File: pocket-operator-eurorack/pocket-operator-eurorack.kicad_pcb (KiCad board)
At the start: 2 copper layers, 70.8 x 128.5 mm, 0 parts

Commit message: kicad silkscreen updated
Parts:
- added G***: LOGO, pocket-operator-eurorack:hook_fill, F.Cu at (31.6, 8.89)
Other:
- outline, holes or cut-outs redrawn

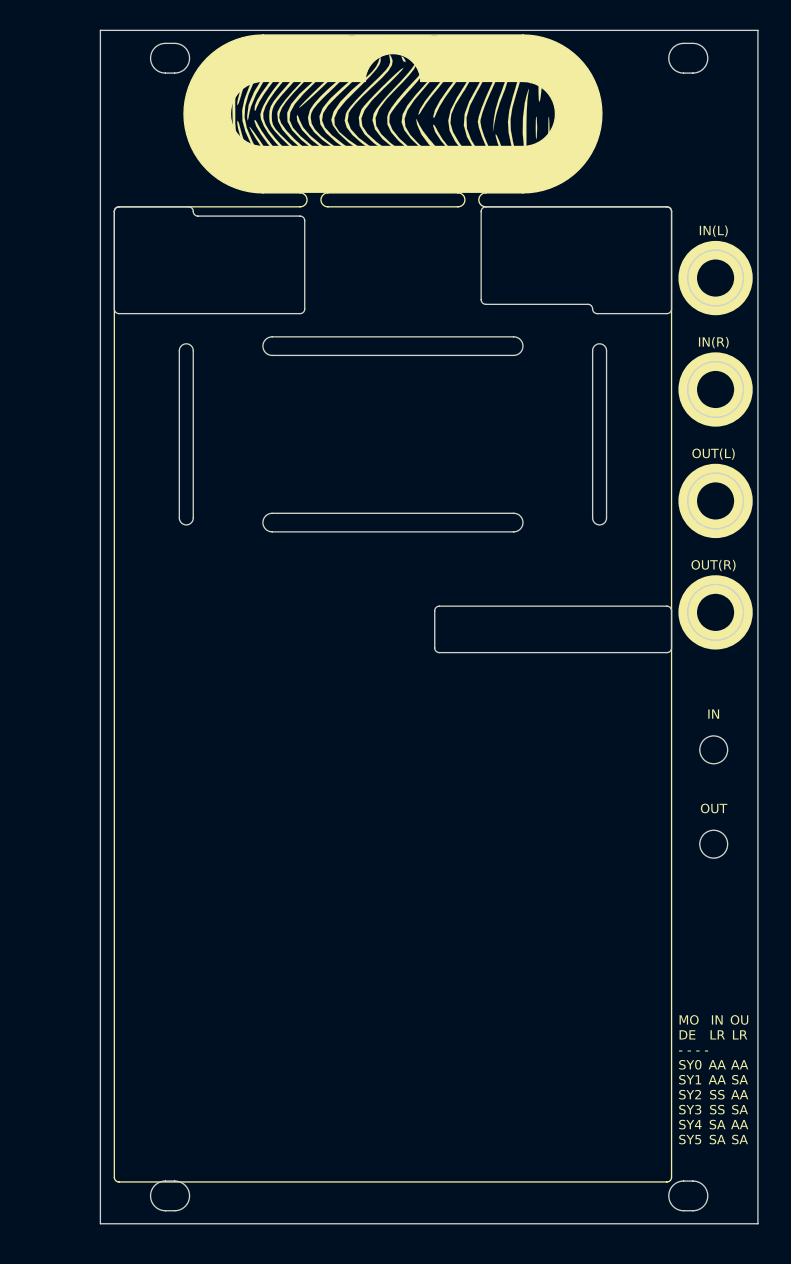
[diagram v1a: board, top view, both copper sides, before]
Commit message: front silkscreen artwork finished
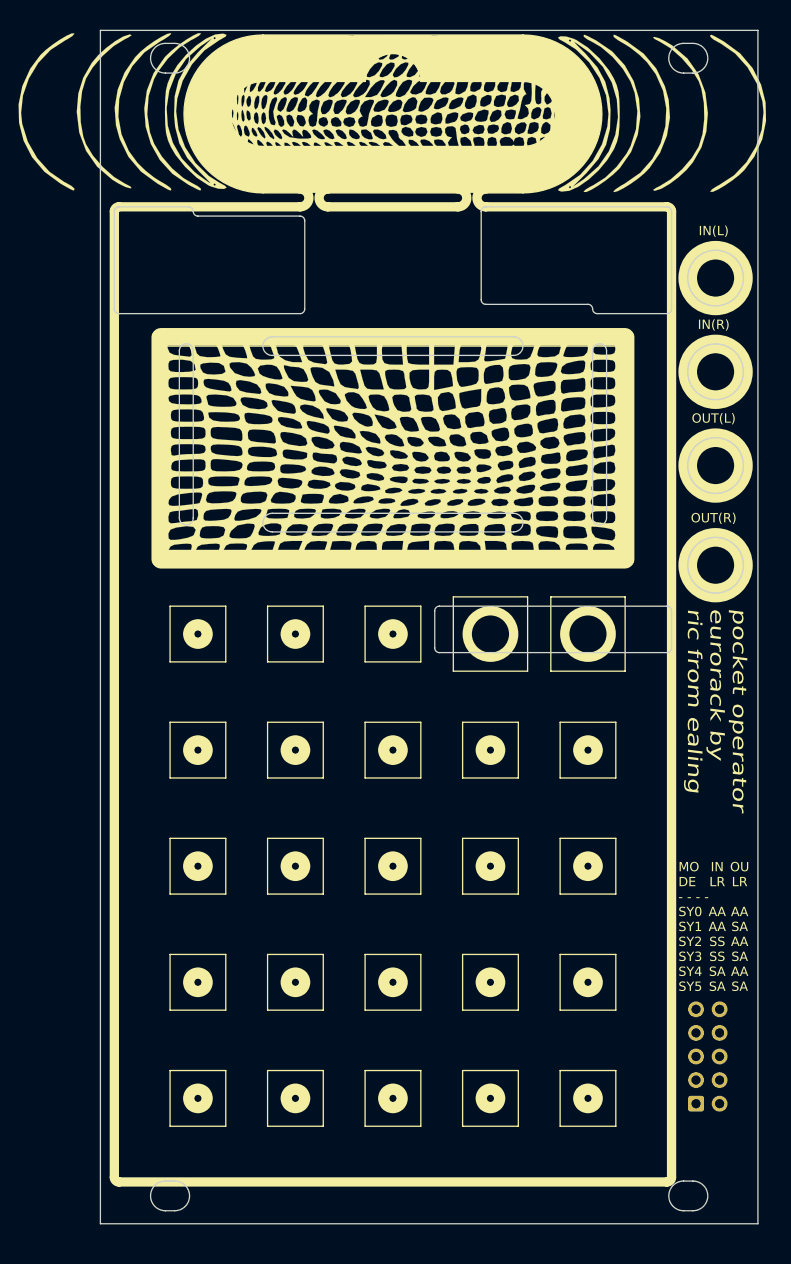
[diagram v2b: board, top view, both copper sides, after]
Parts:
- removed the G*** at (31.6, 8.89)
- added ?: , , F.Cu at (22.2, 12.1)
- added G***: LOGO, pocket-operator-eurorack:screen, F.Cu at (31.1, 45.1)
- added G***: LOGO, pocket-operator-eurorack:side, F.Cu at (60.3, 8.99)
- added G***: LOGO, pocket-operator-eurorack:side, F.Cu at (2.54, 8.72)
- added G***: LOGO, pocket-operator-eurorack:hook_fill_2, F.Cu at (31.8, 8.26)
- added REF**: IDC-Header_2x05_P2.54mm_Vertical, Connector_IDC:IDC-Header_2x05_P2.54mm_Vertical, B.Cu at (64.1, 115.6)
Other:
- outline, holes or cut-outs redrawn
- board text added: "pocket operator eurorack by ric from ealing"
- board text removed: "IN"
- board text removed: "OUT"

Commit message: components selected and placed on board, need to confirm that gnds are connector to each other and that in/out pads are placed correctly
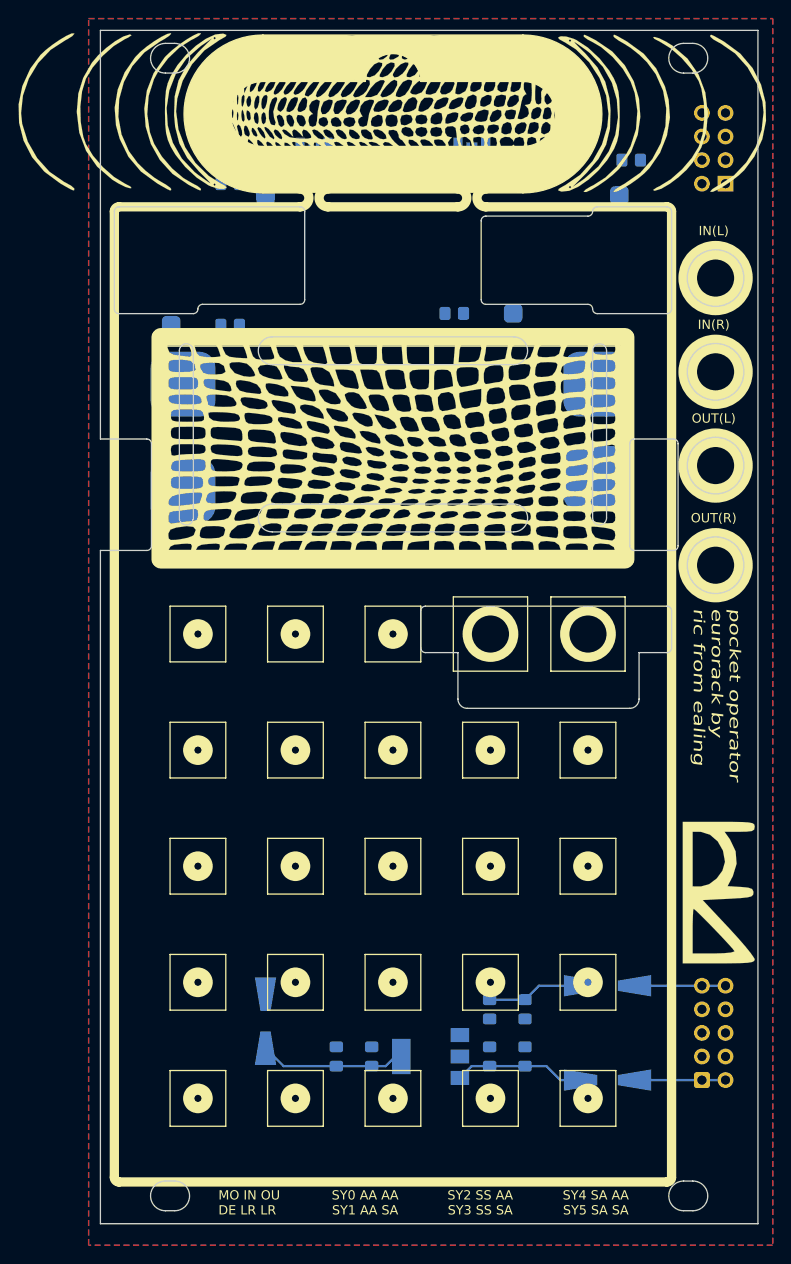
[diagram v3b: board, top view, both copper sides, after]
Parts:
- removed REF**: IDC-Header_2x05_P2.54mm_Vertical, Connector_IDC:IDC-Header_2x05_P2.54mm_Vertical
- added C1: C, Capacitor_SMD:C_0805_2012Metric_Pad1.18x1.45mm_HandSolder, B.Cu at (45.7, 110.5)
- added C2: C, Capacitor_SMD:C_0805_2012Metric_Pad1.18x1.45mm_HandSolder, B.Cu at (45.7, 105.4)
- added C3: C, Capacitor_SMD:C_0805_2012Metric_Pad1.18x1.45mm_HandSolder, B.Cu at (41.9, 110.5)
- added C4: C, Capacitor_SMD:C_0805_2012Metric_Pad1.18x1.45mm_HandSolder, B.Cu at (41.9, 105.4)
- added C5: C, Capacitor_SMD:C_0805_2012Metric_Pad1.18x1.45mm_HandSolder, B.Cu at (29.2, 110.5)
- added C6: C, Capacitor_SMD:C_0805_2012Metric_Pad1.18x1.45mm_HandSolder, B.Cu at (25.4, 110.5)
- added D1: D, Diode_SMD:D_SMA-SMB_Universal_Handsoldering, B.Cu at (54.6, 113.0)
- added D2: D, Diode_SMD:D_SMA-SMB_Universal_Handsoldering, B.Cu at (54.6, 102.9)
- added D3: LED, LED_SMD:LED_Kingbright_APFA3010_3x1.5mm_Horizontal, B.Cu at (23.0, 12.0)
- added D4: LED, LED_SMD:LED_Kingbright_APFA3010_3x1.5mm_Horizontal, B.Cu at (40.0, 12.0)
- added D5: D, Diode_SMD:D_SMA-SMB_Universal_Handsoldering, B.Cu at (17.8, 106.7)
- added G***: LOGO, pocket-operator-eurorack:logo_silk, F.Cu at (66.7, 92.7)
- added G***: LOGO, pocket-operator-eurorack:logo_fcu, F.Cu at (31.6, 24.3)
- added J1: Conn_02x05_Odd_Even, Connector_IDC:IDC-Header_2x05_P2.54mm_Vertical, B.Cu at (64.8, 113.0)
- added J10: Conn_01x01, pocket-operator-eurorack_lib:7mm_solder_pad, B.Cu at (8.89, 38.1)
- added J11: Conn_01x01, pocket-operator-eurorack_lib:7mm_solder_pad, B.Cu at (53.3, 48.3)
- added J12: Conn_01x01, pocket-operator-eurorack_lib:7mm_solder_pad, B.Cu at (8.89, 49.5)
- added J13: Conn_01x01, pocket-operator-eurorack_lib:7mm_solder_pad, B.Cu at (53.3, 38.1)
- added J2: Conn_02x04_Odd_Even, Connector_PinSocket_2.54mm:PinSocket_2x04_P2.54mm_Vertical, B.Cu at (67.3, 16.5)
- added J6: Conn_01x01, pocket-operator-eurorack_lib:2mm_solder_pad, B.Cu at (7.62, 31.8)
- added J7: Conn_01x01, pocket-operator-eurorack_lib:2mm_solder_pad, B.Cu at (55.9, 17.8)
- added J8: Conn_01x01, pocket-operator-eurorack_lib:2mm_solder_pad, B.Cu at (17.8, 17.8)
- added J9: Conn_01x01, pocket-operator-eurorack_lib:2mm_solder_pad, B.Cu at (44.5, 30.5)
- added R1: R, Resistor_SMD:R_0805_2012Metric_Pad1.20x1.40mm_HandSolder, B.Cu at (14.0, 16.5)
- added R2: R, Resistor_SMD:R_0805_2012Metric_Pad1.20x1.40mm_HandSolder, B.Cu at (14.0, 31.8)
- added R3: R, Resistor_SMD:R_0805_2012Metric_Pad1.20x1.40mm_HandSolder, B.Cu at (38.1, 30.5)
- added R4: R, Resistor_SMD:R_0805_2012Metric_Pad1.20x1.40mm_HandSolder, B.Cu at (57.1, 14.0)
- added R5: R, Resistor_SMD:R_0805_2012Metric_Pad1.20x1.40mm_HandSolder, B.Cu at (21.6, 15.2)
- added R6: R, Resistor_SMD:R_0805_2012Metric_Pad1.20x1.40mm_HandSolder, B.Cu at (38.1, 15.2)
- added U1: NCP1117-3.3_SOT223, Package_TO_SOT_SMD:SOT-223-3_TabPin2, B.Cu at (35.6, 110.5)
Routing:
- net Net-(C5-Pad1): track 0.00 -> 15.9 mm
- net +12V: track 0.00 -> 14.1 mm
- net -12V: track 0.00 -> 10.4 mm
- net Net-(D2-Pad1): track 0.00 -> 9.80 mm
- net Net-(D1-Pad2): track 0.00 -> 9.80 mm
- added copper zone on B.Cu, net GND
- added copper zone on F.Cu, net GND
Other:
- outline, holes or cut-outs redrawn
- board text added: "MO IN OU DE LR LR"
- board text added: "SY0 AA AA SY1 AA SA"
- board text added: "SY2 SS AA SY3 SS SA"
- board text added: "SY4 SA AA SY5 SA SA"
- board text removed: "IN LR AA AA SS SS SA SA"
- board text removed: "MO DE - - - - SY0 SY1 SY2 SY3 SY4 SY5"
- board text removed: "OU LR AA SA AA SA AA SA"

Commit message: all tracks tracked, everything added, ready to be reviewed
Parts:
- moved R2 49.3 mm to (59.7, 13.3), turned to 180 degrees
- moved R1 45.7 mm to (59.7, 15.9)
- moved R3 29.2 mm to (59.7, 10.8)
- moved G*** 21.6 mm to (66.7, 114.3)
- moved J10 12.5 mm to (14.0, 49.5)
- moved J12 12.5 mm to (14.0, 38.1)
- moved J11 10.9 mm to (49.5, 38.1)
- moved J13 10.9 mm to (49.5, 48.3)
- moved C1 8.89 mm to (45.7, 101.6)
- moved C2 8.89 mm to (45.7, 96.5)
- moved C3 8.89 mm to (41.9, 101.6)
- moved C4 8.89 mm to (41.9, 96.5)
- moved C5 8.89 mm to (29.2, 101.6)
- moved C6 8.89 mm to (25.4, 101.6)
- moved D1 8.89 mm to (54.6, 104.1)
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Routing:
- net /IN_R: track 0.00 -> 68.5 mm, vias 0 -> 5
- net /IN_L: track 0.00 -> 58.6 mm, vias 0 -> 3
- net /OUT_L: track 0.00 -> 56.6 mm, vias 0 -> 3
- net +3V3: track 0.00 -> 46.9 mm
- net /OUT_R: track 0.00 -> 26.8 mm, vias 0 -> 1
- net Net-(D4-Pad2): track 0.00 -> 3.45 mm
- net Net-(D3-Pad2): track 0.00 -> 3.20 mm
- net Net-(C5-Pad1): track 15.9 -> 18.5 mm
- net +12V: track 14.1 -> 14.7 mm
- added copper zone on B.Cu, net +12V
- added copper zone on B.Cu, net Net-(C5-Pad1)
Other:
- outline, holes or cut-outs redrawn
- board text added: "MUTE"

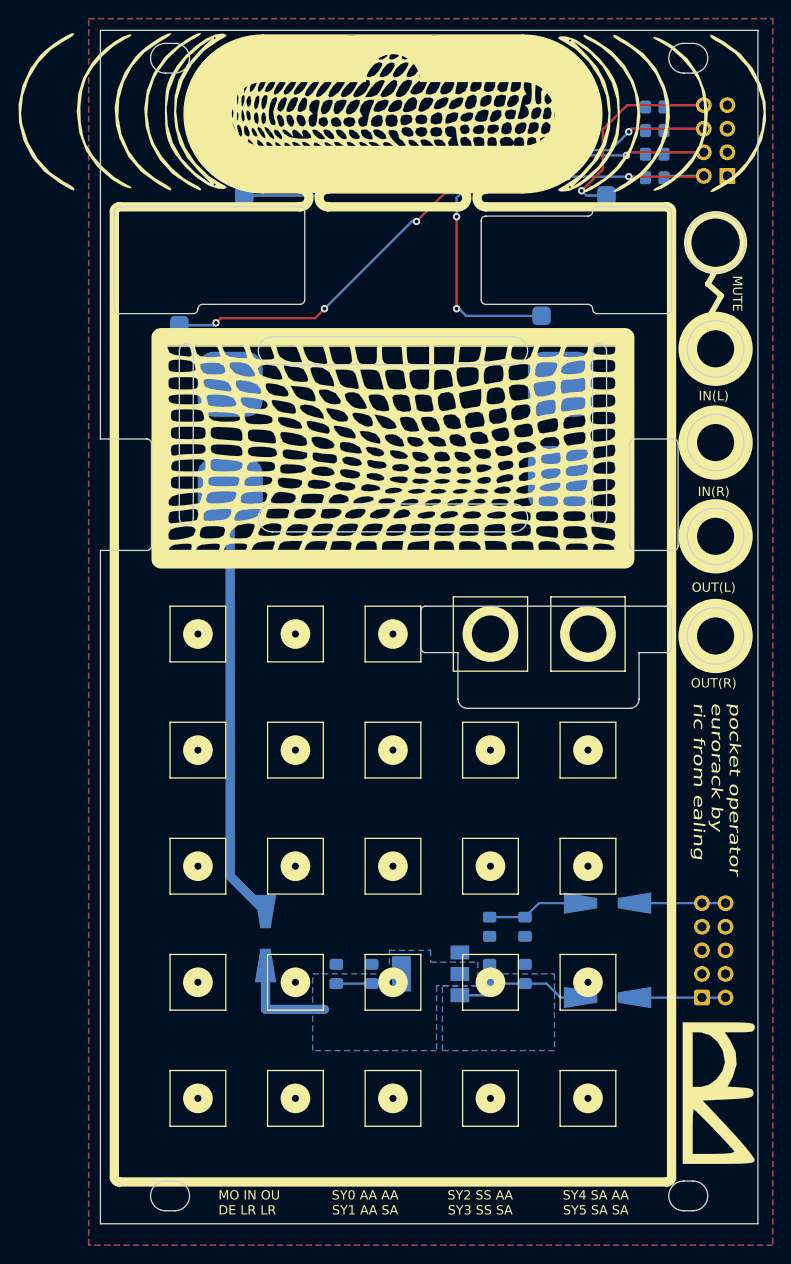
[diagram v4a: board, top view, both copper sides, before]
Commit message: connector board added, main board changed to fit connectors correctly
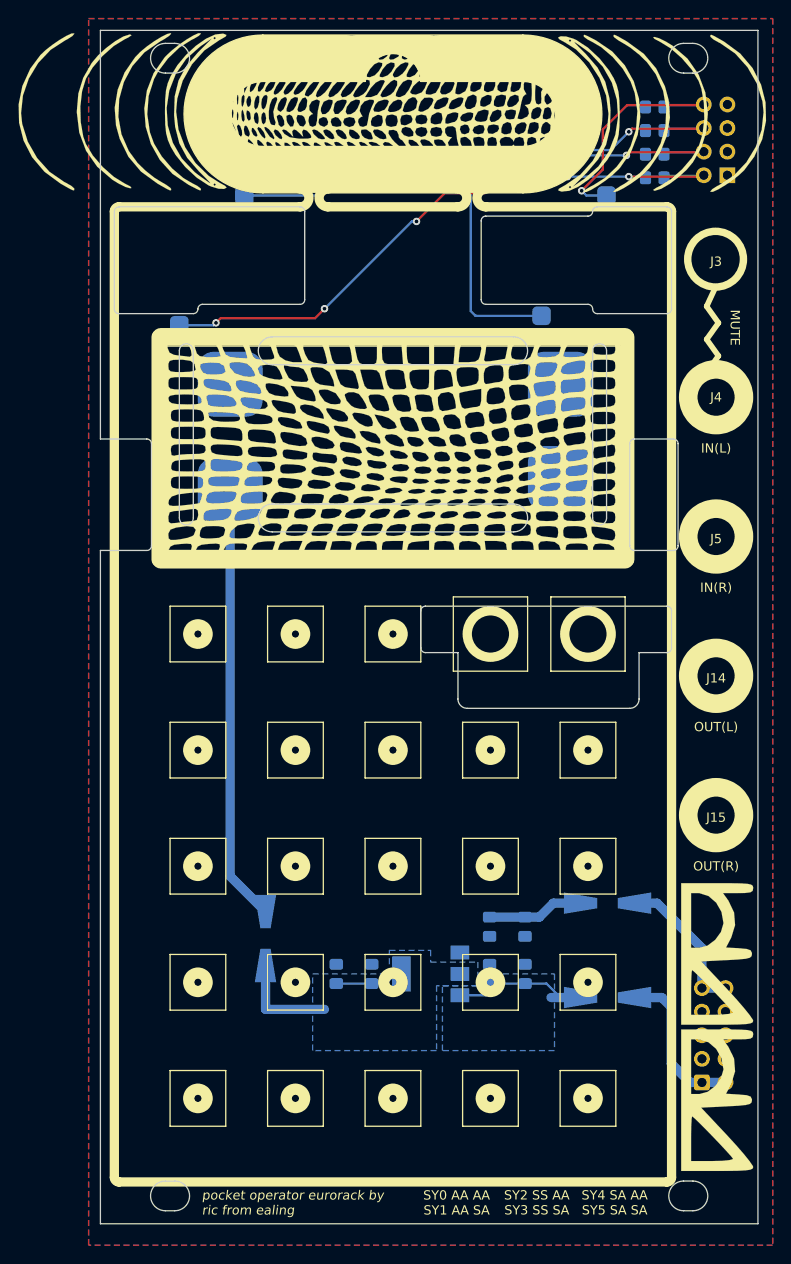
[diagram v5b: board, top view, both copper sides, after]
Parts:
- added G***: LOGO, pocket-operator-eurorack:logo_silk, F.Cu at (66.5, 99.3)
- added J14: Thonkiconn_PJ398SM_panel, mylibs:Thonkiconn_PJ398SM_panel, F.Cu at (66.3, 69.5)
- added J15: Thonkiconn_PJ398SM_panel, mylibs:Thonkiconn_PJ398SM_panel, F.Cu at (66.3, 84.5)
- added J3: SW_6mm_panel, mylibs:SW_6mm_panel, F.Cu at (66.3, 24.6)
- added J4: Thonkiconn_PJ398SM_panel, mylibs:Thonkiconn_PJ398SM_panel, F.Cu at (66.3, 39.5)
- added J5: Thonkiconn_PJ398SM_panel, mylibs:Thonkiconn_PJ398SM_panel, F.Cu at (66.3, 54.5)
- moved J1 9.14 mm to (64.8, 113.3)
- moved G*** 0.78 mm to (66.5, 115.1)
- moved J2 0.07 mm to (67.5, 15.6)
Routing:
- net Net-(D1-Pad2): track 9.80 -> 17.2 mm
- net Net-(D2-Pad1): track 9.80 -> 16.1 mm
- net +12V: track 14.7 -> 17.8 mm
- net /OUT_L: track 56.6 -> 54.6 mm, vias 3 -> 1
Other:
- outline, holes or cut-outs redrawn
- board text removed: "MO IN OU DE LR LR"

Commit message: finished and gerbers sent off for production
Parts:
- removed ?: , 
- added D6: LED, LED_SMD:LED_0805_2012Metric_Pad1.15x1.40mm_HandSolder, B.Cu at (39.4, 111.8)
- added D7: LED, LED_SMD:LED_0805_2012Metric_Pad1.15x1.40mm_HandSolder, B.Cu at (33.0, 111.8)
- added G***: LOGO, pocket-operator-eurorack:logo_small, B.Cu at (39.4, 120.0)
- added G***: LOGO, pocket-operator-eurorack:saka, B.Cu at (26.7, 82.5)
- added G***: LOGO, pocket-operator-eurorack:hook_fill_2, B.Cu at (31.5, 8.64)
- added G***: LOGO, pocket-operator-eurorack:logo_silk, B.Cu at (31.5, 24.8)
- added J16: Conn_01x01, pocket-operator-eurorack_lib:2mm_solder_pad, B.Cu at (39.4, 108.5)
- added J17: Conn_01x01, pocket-operator-eurorack_lib:2mm_solder_pad, B.Cu at (33.0, 108.5)
- added R7: R, Resistor_SMD:R_0805_2012Metric_Pad1.20x1.40mm_HandSolder, B.Cu at (41.9, 111.8)
- added R8: R, Resistor_SMD:R_0805_2012Metric_Pad1.20x1.40mm_HandSolder, B.Cu at (30.5, 111.7)
- added REF**: KiCad-Logo2_5mm_SilkScreen, Symbol:KiCad-Logo2_5mm_SilkScreen, B.Cu at (25.4, 120.0)
- added REF**: WEEE-Logo_4.2x6mm_SilkScreen, Symbol:WEEE-Logo_4.2x6mm_SilkScreen, B.Cu at (48.3, 120.0)
- moved J1 10.5 mm to (67.3, 103.1), turned to 180 degrees
- moved D1 4.49 mm to (51.4, 107.3), turned to 270 degrees
- moved J12 1.03 mm to (14.0, 48.5)
- moved J9 1.02 mm to (47.5, 31.8)
- moved J6 0.50 mm to (9.00, 31.8)
- moved J7 0.50 mm to (54.0, 17.8)
- moved J11 0.40 mm to (14.0, 38.5)
- moved J13 0.40 mm to (49.5, 38.5)
- moved J10 0.24 mm to (49.5, 48.5)
- renumbered J13 to J10, J12 to J11, J10 to J12, J11 to J13
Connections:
- J10 pad 1: Net-(J13-Pad1) -> +3V3
- J11 pad 1: Net-(J12-Pad1) -> GND
- J12 pad 1: +3V3 -> Net-(J12-Pad1)
- J13 pad 1: GND -> Net-(J13-Pad1)
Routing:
- net +3V3: track 46.9 -> 71.3 mm
- net Net-(D2-Pad1): track 16.1 -> 29.1 mm
- net Net-(D1-Pad2): track 17.2 -> 25.0 mm
- net Net-(D7-Pad2): track 0.00 -> 2.56 mm
- net Net-(D6-Pad2): track 0.00 -> 2.55 mm
- net Net-(C5-Pad1): track 18.5 -> 20.8 mm
- net +12V: track 17.8 -> 19.7 mm
- net GND: vias 0 -> 74
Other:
- outline, holes or cut-outs redrawn
- board text added: "-12V GND GND GND +12V"
- board text added: "12V"
- board text added: "3V3"
- board text added: "IN L"
- board text added: "IN R"
- board text added: "OUT L"
- board text added: "OUT R"
- board text added: "Ric from Ealing supports local hero Bukayo Saka"
- board text added: "V+"
- board text added: "V-"
- board text added: "red line"
- board text added: "“Saka is burdened with glorious purpose”"
